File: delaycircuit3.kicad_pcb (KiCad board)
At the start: 2 copper layers, 115.6 x 105.4 mm, 20 parts, among them J1 Screw_Terminal_01x02, J2 Screw_Terminal_01x02, J3 Screw_Terminal_01x02, J5 Screw_Terminal_01x03, J6 Screw_Terminal_01x02, U1 CD4002BE, U2 NE555N, U3 CD4002BE, U4 CD4002BE, U5 CD4002BE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

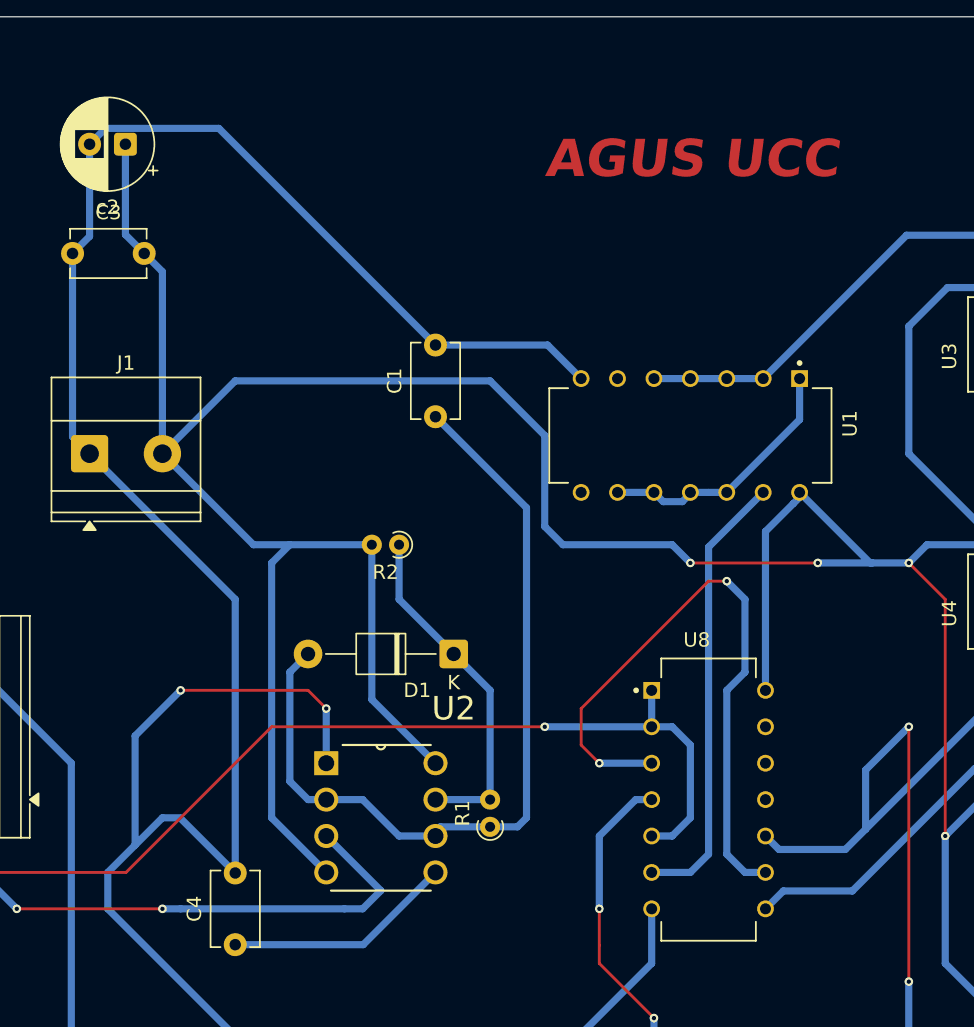
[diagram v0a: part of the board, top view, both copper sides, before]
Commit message: resistencia en seire
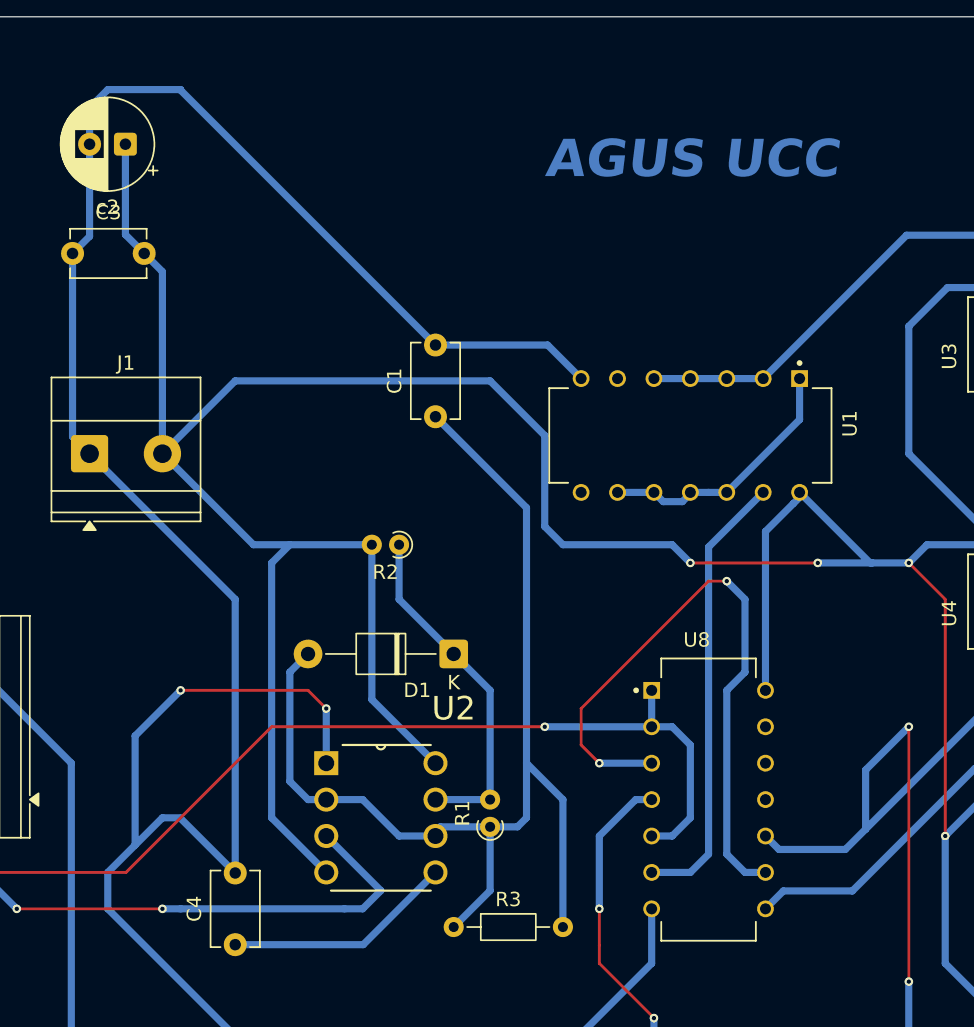
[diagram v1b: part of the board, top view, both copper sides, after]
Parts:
- added R3: 2,7k, Resistor_THT:R_Axial_DIN0204_L3.6mm_D1.6mm_P7.62mm_Horizontal, F.Cu at (174.0, 115.6)
- R1: value 13k -> 1ok
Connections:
- R1 pad 1: Net-(D1-A) -> Net-(R1-Pad1)
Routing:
- net Net-(D1-A): track 58.5 -> 71.0 mm
- net Net-(R1-Pad1): track 0.00 -> 7.49 mm
- net Net-(J1-Pin_1): track 379.4 -> 383.1 mm
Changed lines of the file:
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@@
 	(net 25 "unconnected-(U8-M=~G+H-Pad11)")
 	(net 26 "unconnected-(U8-H-Pad13)")
+	(net 27 "Net-(R1-Pad1)")
 	(footprint "Capacitor_THT:C_Disc_D5.1mm_W3.2mm_P5.00mm"
 		(placed yes)
@@
 		(embedded_fonts no)
 	)
+	(footprint "Resistor_THT:R_Axial_DIN0204_L3.6mm_D1.6mm_P7.62mm_Horizontal"
+		(layer "F.Cu")
+		(at 173.99 115.57)
+		(descr "Resistor, Axial_DIN0204 series, Axial, Horizontal, pin pitch=7.62mm, 0.167W, length*diameter=3.6*1.6mm^2, http://cdn-reichelt.de/documents/datenblatt/B400/1_4W%23YAG.pdf")
+		(tags "Resistor Axial_DIN0204 series Axial Horizontal pin pitch 7.62mm 0.167W length 3.6mm diameter 1.6mm")
+		(property "Reference" "R3"
+			(at 3.81 -1.92 0)
+			(layer "F.SilkS")
+			(effects
+				(font
+					(size 1 1)
+					(thickness 0.15)
+				)
+			)
+		)
+		(property "Value" "2,7k"
+			(at 3.81 1.92 0)
+			(layer "F.Fab")
+			(effects
+				(font
+					(size 1 1)
+					(thickness 0.15)
+				)
+			)
+		)
+		(property "Datasheet" ""
+			(at 0 0 0)
+			(layer "F.Fab")
+			(hide yes)
+			(effects
+				(font
+					(size 1.27 1.27)
+					(thickness 0.15)
+				)
+			)
+		)
+		(property "Description" "Resistor, US symbol"
+			(at 0 0 0)
+			(layer "F.Fab")
+			(hide yes)
+			(effects
+				(font
+					(size 1.27 1.27)
+					(thickness 0.15)
+				)
+			)
+		)
+		(property ki_fp_filters "R_*")
+		(sheetname "/")
+		(sheetfile "delaycircuit3.kicad_sch")
+		(attr through_hole)
+		(fp_line
+			(start 0.94 0)
+			(end 1.89 0)
+			(stroke
+				(width 0.12)
+				(type solid)
+			)
+			(layer "F.SilkS")
+		)
+		(fp_line
+			(start 6.68 0)
+			(end 5.73 0)
+			(stroke
+				(width 0.12)
+				(type solid)
+			)
+			(layer "F.SilkS")
+		)
+		(fp_rect
+			(start 1.89 -0.92)
+			(end 5.73 0.92)
+			(stroke
+				(width 0.12)
+				(type solid)
+			)
+			(fill no)
+			(layer "F.SilkS")
+		)
+		(fp_rect
+			(start -0.95 -1.05)
+			(end 8.57 1.05)
+			(stroke
+				(width 0.05)
+				(type solid)
+			)
+			(fill no)
+			(layer "F.CrtYd")
+		)
+		(fp_line
+			(start 0 0)
+			(end 2.01 0)
+			(stroke
+				(width 0.1)
+				(type solid)
+			)
+			(layer "F.Fab")
+		)
+		(fp_line
+			(start 7.62 0)
+			(end 5.61 0)
+			(stroke
+				(width 0.1)
+				(type solid)
+			)
+			(layer "F.Fab")
+		)
+		(fp_rect
+			(start 2.01 -0.8)
+			(end 5.61 0.8)
+			(stroke
+				(width 0.1)
+				(type solid)
+			)
+			(fill no)
+			(layer "F.Fab")
+		)
+		(fp_text user "${REFERENCE}"
+			(at 3.81 0 0)
+			(layer "F.Fab")
+			(effects
+				(font
+					(size 0.72 0.72)
+					(thickness 0.108)
+				)
+			)
+		)
+		(pad "1" thru_hole circle
+			(at 0 0)
+			(size 1.4 1.4)
+			(drill 0.7)
+			(layers "*.Cu" "*.Mask")
+			(remove_unused_layers no)
+			(net 27 "Net-(R1-Pad1)")
+			(pintype "passive")
+		)
+		(pad "2" thru_hole circle
+			(at 7.62 0)
+			(size 1.4 1.4)
+			(drill 0.7)
+			(layers "*.Cu" "*.Mask")
+			(remove_unused_layers no)
+			(net 2 "Net-(D1-A)")
+			(pintype "passive")
+		)
+		(embedded_fonts no)
+		(model "${KICAD9_3DMODEL_DIR}/Resistor_THT.3dshapes/R_Axial_DIN0204_L3.6mm_D1.6mm_P7.62mm_Horizontal.step"
+			(offset
+				(xyz 0 0 0)
+			)
+			(scale
+				(xyz 1 1 1)
+			)
+			(rotate
+				(xyz 0 0 0)
+			)
+		)
+	)
 	(footprint "TerminalBlock_Phoenix:TerminalBlock_Phoenix_MKDS-1,5-2-5.08_1x02_P5.08mm_Horizontal"
 		(placed yes)
@@
 			)
 		)
-		(property "Value" "13k"
+		(property "Value" "1ok"
 			(at 0.95 1.92 90)
 			(layer "F.Fab")
@@
 			(layers "*.Cu" "*.Mask")
 			(remove_unused_layers no)
-			(net 2 "Net-(D1-A)")
+			(net 27 "Net-(R1-Pad1)")
 			(pintype "passive")
 		)
@@
 	(gr_text "AGUS UCC"
 		(at 180.34 63.5 0)
-		(layer "F.Cu")
+		(layer "B.Cu")
 		(effects
 			(font
@@
 	)
 	(segment
-		(start 157.6057 59.8557)
-		(end 172.72 74.97)
-		(width 0.5)
-		(layer "B.Cu")
-		(net 1)
-	)
-	(segment
 		(start 159.86 124.3)
 		(end 159.385 123.825)
@@
 	)
 	(segment
+		(start 148.59 58.42)
+		(end 149.86 57.15)
+		(width 0.5)
+		(layer "B.Cu")
+		(net 1)
+	)
+	(segment
 		(start 231.14 129.7)
 		(end 234.79 129.7)
@@
 	)
 	(segment
+		(start 149.86 57.15)
+		(end 154.94 57.15)
+		(width 0.5)
+		(layer "B.Cu")
+		(net 1)
+	)
+	(segment
 		(start 210.815 138.6025)
 		(end 222.2375 138.6025)
@@
 	)
 	(segment
+		(start 154.94 57.19)
+		(end 172.72 74.97)
+		(width 0.5)
+		(layer "B.Cu")
+		(net 1)
+	)
+	(segment
+		(start 154.94 57.15)
+		(end 154.94 57.19)
+		(width 0.5)
+		(layer "B.Cu")
+		(net 1)
+	)
+	(segment
 		(start 210.815 151.125)
 		(end 209.54 152.4)
@@
 	)
 	(segment
-		(start 163.83 137.16)
-		(end 163.83 128.11)
+		(start 148.59 60.96)
+		(end 148.59 58.42)
 		(width 0.5)
 		(layer "B.Cu")
@@
 	)
 	(segment
-		(start 148.59 60.96)
-		(end 149.6943 59.8557)
+		(start 163.83 137.16)
+		(end 163.83 128.11)
 		(width 0.5)
 		(layer "B.Cu")
@@
 	)
 	(segment
-		(start 149.6943 59.8557)
-		(end 157.6057 59.8557)
+		(start 179.07 107.95)
+		(end 179.07 104.14)
 		(width 0.5)
 		(layer "B.Cu")
-		(net 1)
+		(net 2)
 	)
 	(segment
@@
 	)
 	(segment
-		(start 179.07 107.95)
+		(start 179.07 104.14)
 		(end 179.07 86.32)
 		(width 0.5)
@@
 	)
 	(segment
+		(start 181.61 115.57)
+		(end 181.61 106.68)
+		(width 0.5)
+		(layer "B.Cu")
+		(net 2)
+	)
+	(segment
 		(start 162.56 105.41)
 		(end 162.56 97.79)
@@
 	)
 	(segment
+		(start 181.61 106.68)
+		(end 179.07 104.14)
+		(width 0.5)
+		(layer "B.Cu")
+		(net 2)
+	)
+	(segment
 		(start 176.53 108.58)
 		(end 178.44 108.58)
@@
 		(net 24)
 	)
+	(segment
+		(start 173.99 115.57)
+		(end 176.53 113.03)
+		(width 0.5)
+		(layer "B.Cu")
+		(net 27)
+	)
+	(segment
+		(start 176.53 113.03)
+		(end 176.53 109.131)
+		(width 0.5)
+		(layer "B.Cu")
+		(net 27)
+	)
 	(embedded_fonts no)
